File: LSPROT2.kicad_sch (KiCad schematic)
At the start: 5 parts, among them U3 VNLD5160TR-E

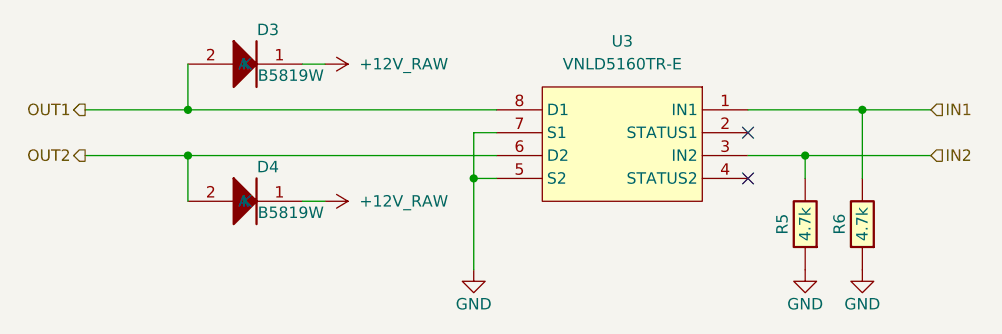
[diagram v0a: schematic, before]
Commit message: add submodules for ign and inj + flyback protected output
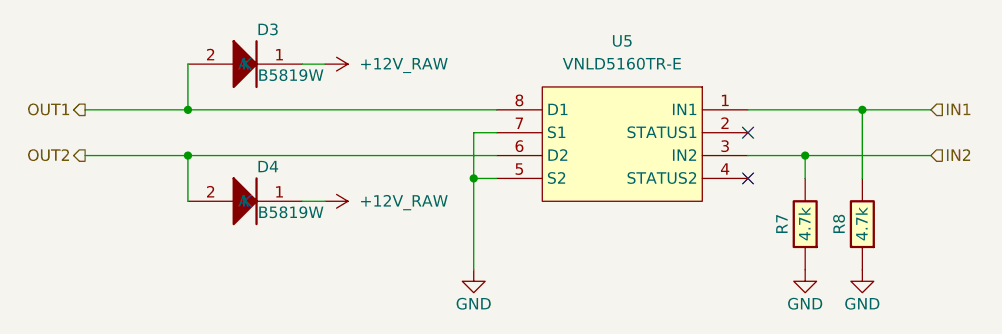
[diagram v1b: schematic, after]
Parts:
- D3, D4: footprint hellen-one-common:SOD-123 -> footprints:SOD-123
- R7: renamed from R5; footprint hellen-one-common:R0603 -> footprints:R0603
- R8: renamed from R6; footprint hellen-one-common:R0603 -> footprints:R0603
- renumbered U3 to U5
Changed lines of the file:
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@@
 		(on_board yes)
 		(dnp no)
-		(property "Reference" "U3"
+		(property "Reference" "U5"
 			(at 153.67 81.28 0)
 			(effects
@@
 			(project "EP91Starlet"
 				(path "/10fbc709-889c-4565-8161-129ca9f0b73f/1ff2d20b-dc8b-4917-a06e-679ad9dbc3b7"
-					(reference "U3")
-					(unit 1)
-				)
-				(path "/10fbc709-889c-4565-8161-129ca9f0b73f/c0449a5d-f20c-4d0f-b0f4-b41fc2a2c2f9"
-					(reference "U1")
+					(reference "U5")
+					(unit 1)
+				)
+				(path "/10fbc709-889c-4565-8161-129ca9f0b73f/c0449a5d-f20c-4d0f-b0f4-b41fc2a2c2f9"
+					(reference "U4")
 					(unit 1)
 				)
@@
 			)
 		)
-		(property "Footprint" "hellen-one-common:SOD-123"
+		(property "Footprint" "footprints:SOD-123"
 			(at 113.03 92.71 0)
 			(effects
@@
 		(on_board yes)
 		(dnp no)
-		(property "Reference" "#PWR1"
+		(property "Reference" "#PWR12"
 			(at 116.84 83.82 0)
 			(effects
@@
 			(project "EP91Starlet"
 				(path "/10fbc709-889c-4565-8161-129ca9f0b73f/1ff2d20b-dc8b-4917-a06e-679ad9dbc3b7"
-					(reference "#PWR1")
-					(unit 1)
-				)
-				(path "/10fbc709-889c-4565-8161-129ca9f0b73f/c0449a5d-f20c-4d0f-b0f4-b41fc2a2c2f9"
-					(reference "#PWR?")
+					(reference "#PWR12")
+					(unit 1)
+				)
+				(path "/10fbc709-889c-4565-8161-129ca9f0b73f/c0449a5d-f20c-4d0f-b0f4-b41fc2a2c2f9"
+					(reference "#PWR7")
 					(unit 1)
 				)
@@
 		(on_board yes)
 		(dnp no)
-		(property "Reference" "#PWR3"
+		(property "Reference" "#PWR14"
 			(at 137.16 113.03 0)
 			(effects
@@
 			(project "EP91Starlet"
 				(path "/10fbc709-889c-4565-8161-129ca9f0b73f/1ff2d20b-dc8b-4917-a06e-679ad9dbc3b7"
-					(reference "#PWR3")
-					(unit 1)
-				)
-				(path "/10fbc709-889c-4565-8161-129ca9f0b73f/c0449a5d-f20c-4d0f-b0f4-b41fc2a2c2f9"
-					(reference "#PWR?")
+					(reference "#PWR14")
+					(unit 1)
+				)
+				(path "/10fbc709-889c-4565-8161-129ca9f0b73f/c0449a5d-f20c-4d0f-b0f4-b41fc2a2c2f9"
+					(reference "#PWR9")
 					(unit 1)
 				)
@@
 		(on_board yes)
 		(dnp no)
-		(property "Reference" "R6"
+		(property "Reference" "R8"
 			(at 177.8 101.6 0)
 			(effects
@@
 			)
 		)
-		(property "Footprint" "hellen-one-common:R0603"
+		(property "Footprint" "footprints:R0603"
 			(at 184.15 102.87 0)
 			(effects
@@
 			(project "EP91Starlet"
 				(path "/10fbc709-889c-4565-8161-129ca9f0b73f/1ff2d20b-dc8b-4917-a06e-679ad9dbc3b7"
+					(reference "R8")
+					(unit 1)
+				)
+				(path "/10fbc709-889c-4565-8161-129ca9f0b73f/c0449a5d-f20c-4d0f-b0f4-b41fc2a2c2f9"
 					(reference "R6")
-					(unit 1)
-				)
-				(path "/10fbc709-889c-4565-8161-129ca9f0b73f/c0449a5d-f20c-4d0f-b0f4-b41fc2a2c2f9"
-					(reference "R1")
 					(unit 1)
 				)
@@
 		(on_board yes)
 		(dnp no)
-		(property "Reference" "R5"
+		(property "Reference" "R7"
 			(at 171.45 101.6 0)
 			(effects
@@
 			)
 		)
-		(property "Footprint" "hellen-one-common:R0603"
+		(property "Footprint" "footprints:R0603"
 			(at 177.8 102.87 0)
 			(effects
@@
 			(project "EP91Starlet"
 				(path "/10fbc709-889c-4565-8161-129ca9f0b73f/1ff2d20b-dc8b-4917-a06e-679ad9dbc3b7"
+					(reference "R7")
+					(unit 1)
+				)
+				(path "/10fbc709-889c-4565-8161-129ca9f0b73f/c0449a5d-f20c-4d0f-b0f4-b41fc2a2c2f9"
 					(reference "R5")
-					(unit 1)
-				)
-				(path "/10fbc709-889c-4565-8161-129ca9f0b73f/c0449a5d-f20c-4d0f-b0f4-b41fc2a2c2f9"
-					(reference "R2")
 					(unit 1)
 				)
@@
 		(on_board yes)
 		(dnp no)
-		(property "Reference" "#PWR5"
+		(property "Reference" "#PWR16"
 			(at 180.34 113.03 0)
 			(effects
@@
 			(project "EP91Starlet"
 				(path "/10fbc709-889c-4565-8161-129ca9f0b73f/1ff2d20b-dc8b-4917-a06e-679ad9dbc3b7"
-					(reference "#PWR5")
-					(unit 1)
-				)
-				(path "/10fbc709-889c-4565-8161-129ca9f0b73f/c0449a5d-f20c-4d0f-b0f4-b41fc2a2c2f9"
-					(reference "#PWR?")
+					(reference "#PWR16")
+					(unit 1)
+				)
+				(path "/10fbc709-889c-4565-8161-129ca9f0b73f/c0449a5d-f20c-4d0f-b0f4-b41fc2a2c2f9"
+					(reference "#PWR11")
 					(unit 1)
 				)
@@
 			)
 		)
-		(property "Footprint" "hellen-one-common:SOD-123"
+		(property "Footprint" "footprints:SOD-123"
 			(at 113.03 77.47 0)
 			(effects
@@
 		(on_board yes)
 		(dnp no)
-		(property "Reference" "#PWR2"
+		(property "Reference" "#PWR13"
 			(at 116.84 99.06 0)
 			(effects
@@
 			(project "EP91Starlet"
 				(path "/10fbc709-889c-4565-8161-129ca9f0b73f/1ff2d20b-dc8b-4917-a06e-679ad9dbc3b7"
-					(reference "#PWR2")
-					(unit 1)
-				)
-				(path "/10fbc709-889c-4565-8161-129ca9f0b73f/c0449a5d-f20c-4d0f-b0f4-b41fc2a2c2f9"
-					(reference "#PWR?")
+					(reference "#PWR13")
+					(unit 1)
+				)
+				(path "/10fbc709-889c-4565-8161-129ca9f0b73f/c0449a5d-f20c-4d0f-b0f4-b41fc2a2c2f9"
+					(reference "#PWR8")
 					(unit 1)
 				)
@@
 		(on_board yes)
 		(dnp no)
-		(property "Reference" "#PWR4"
+		(property "Reference" "#PWR15"
 			(at 173.99 113.03 0)
 			(effects
@@
 			(project "EP91Starlet"
 				(path "/10fbc709-889c-4565-8161-129ca9f0b73f/1ff2d20b-dc8b-4917-a06e-679ad9dbc3b7"
-					(reference "#PWR4")
-					(unit 1)
-				)
-				(path "/10fbc709-889c-4565-8161-129ca9f0b73f/c0449a5d-f20c-4d0f-b0f4-b41fc2a2c2f9"
-					(reference "#PWR?")
-					(unit 1)
-				)
+					(reference "#PWR15")
+					(unit 1)
+				)
+				(path "/10fbc709-889c-4565-8161-129ca9f0b73f/c0449a5d-f20c-4d0f-b0f4-b41fc2a2c2f9"
+					(reference "#PWR10")
+					(unit 1)
+				)
